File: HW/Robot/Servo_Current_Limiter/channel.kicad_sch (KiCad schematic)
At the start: 7 parts, among them J12 1x1 2.54mm male, J13 1x3 2.54mm male, Q7 IRF4905, Q8 BC548

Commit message: Something done.
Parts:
- added JP3: 1x2 2.54mm male, Connector_PinHeader_2.54mm:PinHeader_1x02_P2.54mm_Vertical, symbol Jumper:Jumper_2_Open
- added R25: 100k, For_Rasterboard:R_Axial_DIN0207_L6.3mm_D2.5mm_P7.62mm_Horizontal, symbol Device:R
- R19: value 220 -> 1k
- RV4: value 250 -> 1k
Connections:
- net +5V: now also JP3.1 (A), R25.1
- net DISABLE: now also R25.2
- net P: now also JP3.2 (B)
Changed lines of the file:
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@@
   (junction (at 206.375 82.55) (diameter 0) (color 0 0 0 0)
   )
+  (junction (at 170.18 35.56) (diameter 0) (color 0 0 0 0)
+  )
   (junction (at 177.8 43.18) (diameter 0) (color 0 0 0 0)
   )
   (junction (at 152.4 77.47) (diameter 0) (color 0 0 0 0)
   )
+  (junction (at 164.465 35.56) (diameter 0) (color 0 0 0 0)
+  )
+  (junction (at 184.785 35.56) (diameter 0) (color 0 0 0 0)
+  )
+  (junction (at 164.465 43.18) (diameter 0) (color 0 0 0 0)
+  )
   (wire (pts (xy 255.905 78.74) (xy 249.555 78.74))
     (stroke (width 0) (type default) (color 0 0 0 0))
   )
-  (wire (pts (xy 182.88 35.56) (xy 187.96 35.56))
+  (wire (pts (xy 182.88 35.56) (xy 184.785 35.56))
+    (stroke (width 0) (type default) (color 0 0 0 0))
+  )
+  (wire (pts (xy 164.465 35.56) (xy 170.18 35.56))
+    (stroke (width 0) (type default) (color 0 0 0 0))
+  )
+  (wire (pts (xy 182.245 22.225) (xy 184.785 22.225))
     (stroke (width 0) (type default) (color 0 0 0 0))
   )
@@
     (stroke (width 0) (type default) (color 0 0 0 0))
   )
+  (wire (pts (xy 184.785 22.225) (xy 184.785 35.56))
+    (stroke (width 0) (type default) (color 0 0 0 0))
+  )
   (wire (pts (xy 206.375 82.55) (xy 233.045 82.55))
     (stroke (width 0) (type default) (color 0 0 0 0))
@@
     (stroke (width 0) (type default) (color 0 0 0 0))
   )
+  (wire (pts (xy 170.18 35.56) (xy 172.72 35.56))
+    (stroke (width 0) (type default) (color 0 0 0 0))
+  )
   (wire (pts (xy 133.35 81.28) (xy 133.35 85.09))
     (stroke (width 0) (type default) (color 0 0 0 0))
@@
     (stroke (width 0) (type default) (color 0 0 0 0))
   )
+  (wire (pts (xy 164.465 43.18) (xy 177.8 43.18))
+    (stroke (width 0) (type default) (color 0 0 0 0))
+  )
   (wire (pts (xy 195.58 35.56) (xy 200.66 35.56))
     (stroke (width 0) (type default) (color 0 0 0 0))
   )
-  (wire (pts (xy 168.91 35.56) (xy 172.72 35.56))
+  (wire (pts (xy 172.085 22.225) (xy 170.18 22.225))
+    (stroke (width 0) (type default) (color 0 0 0 0))
+  )
+  (wire (pts (xy 158.115 35.56) (xy 164.465 35.56))
     (stroke (width 0) (type default) (color 0 0 0 0))
   )
@@
     (stroke (width 0) (type default) (color 0 0 0 0))
   )
+  (wire (pts (xy 170.18 22.225) (xy 170.18 35.56))
+    (stroke (width 0) (type default) (color 0 0 0 0))
+  )
   (wire (pts (xy 133.35 71.12) (xy 133.35 73.66))
     (stroke (width 0) (type default) (color 0 0 0 0))
@@
     (stroke (width 0) (type default) (color 0 0 0 0))
   )
-  (wire (pts (xy 121.92 43.18) (xy 177.8 43.18))
+  (wire (pts (xy 121.92 43.18) (xy 164.465 43.18))
+    (stroke (width 0) (type default) (color 0 0 0 0))
+  )
+  (wire (pts (xy 184.785 35.56) (xy 187.96 35.56))
     (stroke (width 0) (type default) (color 0 0 0 0))
   )
@@
     (effects (font (size 1.27 1.27)) (justify right))
   )
+  (symbol (lib_id "Device:R") (at 164.465 39.37 0) (unit 1)
+    (in_bom yes) (on_board yes)
+    (property "Reference" "R25" (id 0) (at 159.2072 39.37 90))
+    (property "Value" "100k" (id 1) (at 161.5186 39.37 90))
+    (property "Footprint" "For_Rasterboard:R_Axial_DIN0207_L6.3mm_D2.5mm_P7.62mm_Horizontal" (id 2) (at 162.687 39.37 90)
+      (effects (font (size 1.27 1.27)) hide)
+    )
+    (property "Datasheet" "~" (id 3) (at 164.465 39.37 0)
+      (effects (font (size 1.27 1.27)) hide)
+    )
+    (pin "1")
+    (pin "2")
+  )
+  (symbol (lib_id "Jumper:Jumper_2_Open") (at 177.165 22.225 0) (unit 1)
+    (in_bom yes) (on_board yes) (fields_autoplaced)
+    (property "Reference" "JP3" (id 0) (at 177.165 15.24 0))
+    (property "Value" "1x2 2.54mm male" (id 1) (at 177.165 17.78 0))
+    (property "Footprint" "Connector_PinHeader_2.54mm:PinHeader_1x02_P2.54mm_Vertical" (id 2) (at 177.165 22.225 0)
+      (effects (font (size 1.27 1.27)) hide)
+    )
+    (property "Datasheet" "~" (id 3) (at 177.165 22.225 0)
+      (effects (font (size 1.27 1.27)) hide)
+    )
+    (pin "1")
+    (pin "2")
+  )
   (symbol (lib_id "power:+5V") (at 133.35 60.96 0) (unit 1)
     (in_bom yes) (on_board yes) (fields_autoplaced)
@@
     (pin "1")
   )
-  (symbol (lib_id "power:+5V") (at 168.91 35.56 90) (unit 1)
-    (in_bom yes) (on_board yes)
-    (property "Reference" "#PWR028" (id 0) (at 172.72 35.56 0)
-      (effects (font (size 1.27 1.27)) hide)
-    )
-    (property "Value" "+5V" (id 1) (at 165.6588 35.179 90)
+  (symbol (lib_id "power:+5V") (at 158.115 35.56 90) (unit 1)
+    (in_bom yes) (on_board yes)
+    (property "Reference" "#PWR028" (id 0) (at 161.925 35.56 0)
+      (effects (font (size 1.27 1.27)) hide)
+    )
+    (property "Value" "+5V" (id 1) (at 154.8638 35.179 90)
       (effects (font (size 1.27 1.27)) (justify left))
     )
-    (property "Footprint" "" (id 2) (at 168.91 35.56 0)
-      (effects (font (size 1.27 1.27)) hide)
-    )
-    (property "Datasheet" "" (id 3) (at 168.91 35.56 0)
+    (property "Footprint" "" (id 2) (at 158.115 35.56 0)
+      (effects (font (size 1.27 1.27)) hide)
+    )
+    (property "Datasheet" "" (id 3) (at 158.115 35.56 0)
       (effects (font (size 1.27 1.27)) hide)
     )
@@
     (in_bom yes) (on_board yes)
     (property "Reference" "R19" (id 0) (at 128.0922 67.31 90))
-    (property "Value" "220" (id 1) (at 130.4036 67.31 90))
+    (property "Value" "1k" (id 1) (at 130.4036 67.31 90))
     (property "Footprint" "For_Rasterboard:R_Axial_DIN0207_L6.3mm_D2.5mm_Pinf_Horizontal" (id 2) (at 131.572 67.31 90)
       (effects (font (size 1.27 1.27)) hide)
@@
       (effects (font (size 1.27 1.27)) (justify right))
     )
-    (property "Value" "250" (id 1) (at 130.81 78.7399 0)
+    (property "Value" "1k" (id 1) (at 130.81 78.7399 0)
       (effects (font (size 1.27 1.27)) (justify right))
     )

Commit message: Working.
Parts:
- removed Q8: BC548, For_Rasterboard:TO-92_Inline_inf, symbol Servo_Current_Limiter-cache:BC548
- added R7: 1k, For_Rasterboard:R_Axial_DIN0207_L6.3mm_D2.5mm_Pinf_Horizontal, symbol Device:R
- added U1: LM324, Package_DIP:DIP-14_W7.62mm, symbol Amplifier_Operational:LM324
- renumbered JP3 to JP5, R25 to R43
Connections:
- net DISABLE: now also J12.1, RV4.2, U1.6 (-); no longer Q7.1 (G), R43.2
- net GND: now also R7.2
- net OUT: now also U1.5 (+)
- new net CTRL: Q7.1 (G), R43.2, R7.1, U1.7
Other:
- moved on the sheet: J12, R19, RV4

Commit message: Corrections.
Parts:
- R1: renamed from R19; footprint For_Rasterboard:R_Axial_DIN0207_L6.3mm_D2.5mm_Pinf_Horizontal -> For_Rasterboard:R_Axial_DIN0207_L6.3mm_D2.5mm_P5.08mm_Vertical
- renumbered J12 to J3, J13 to J4, JP5 to JP2, Q7 to Q1, R20 to R2, R43 to R25, RV4 to RV1
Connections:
- net DISABLE renamed N_DISABLE
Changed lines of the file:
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@@
     (effects (font (size 1.27 1.27)) (justify left bottom))
   )
-  (label "DISABLE" (at 117.475 111.125 180)
+  (label "N_DISABLE" (at 117.475 111.125 180)
     (effects (font (size 1.27 1.27)) (justify right bottom))
   )
@@
     (effects (font (size 1.27 1.27)) (justify left bottom))
   )
-  (hierarchical_label "DISABLE" (shape input) (at 102.87 111.125 180)
+  (hierarchical_label "N_DISABLE" (shape input) (at 102.87 111.125 180)
     (effects (font (size 1.27 1.27)) (justify right))
   )
@@
   (symbol (lib_id "Device:R") (at 164.465 39.37 0) (unit 1)
     (in_bom yes) (on_board yes)
-    (property "Reference" "R43" (id 0) (at 159.2072 39.37 90))
+    (property "Reference" "R25" (id 0) (at 159.2072 39.37 90))
     (property "Value" "100k" (id 1) (at 161.5186 39.37 90))
     (property "Footprint" "For_Rasterboard:R_Axial_DIN0207_L6.3mm_D2.5mm_P7.62mm_Horizontal" (id 2) (at 162.687 39.37 90)
@@
   (symbol (lib_id "Jumper:Jumper_2_Open") (at 177.165 22.225 0) (unit 1)
     (in_bom yes) (on_board yes) (fields_autoplaced)
-    (property "Reference" "JP5" (id 0) (at 177.165 15.24 0))
+    (property "Reference" "JP2" (id 0) (at 177.165 15.24 0))
     (property "Value" "1x2 2.54mm male" (id 1) (at 177.165 17.78 0))
     (property "Footprint" "Connector_PinHeader_2.54mm:PinHeader_1x02_P2.54mm_Vertical" (id 2) (at 177.165 22.225 0)
@@
   (symbol (lib_id "power:+5V") (at 107.95 68.58 0) (unit 1)
     (in_bom yes) (on_board yes) (fields_autoplaced)
-    (property "Reference" "#PWR026" (id 0) (at 107.95 72.39 0)
+    (property "Reference" "#PWR011" (id 0) (at 107.95 72.39 0)
       (effects (font (size 1.27 1.27)) hide)
     )
@@
   (symbol (lib_id "power:+5V") (at 158.115 35.56 90) (unit 1)
     (in_bom yes) (on_board yes)
-    (property "Reference" "#PWR028" (id 0) (at 161.925 35.56 0)
+    (property "Reference" "#PWR013" (id 0) (at 161.925 35.56 0)
       (effects (font (size 1.27 1.27)) hide)
     )
@@
   (symbol (lib_id "Connector:TestPoint") (at 127 82.55 0) (unit 1)
     (in_bom yes) (on_board yes)
-    (property "Reference" "J12" (id 0) (at 127 73.66 0))
+    (property "Reference" "J3" (id 0) (at 127 73.66 0))
     (property "Value" "1x1 2.54mm male" (id 1) (at 127 76.2 0))
     (property "Footprint" "Connector_PinHeader_2.54mm:PinHeader_1x01_P2.54mm_Vertical" (id 2) (at 127 82.55 0)
@@
   (symbol (lib_id "Device:R") (at 107.95 74.93 0) (unit 1)
     (in_bom yes) (on_board yes)
-    (property "Reference" "R19" (id 0) (at 102.6922 74.93 90))
+    (property "Reference" "R1" (id 0) (at 102.6922 74.93 90))
     (property "Value" "1k" (id 1) (at 105.0036 74.93 90))
-    (property "Footprint" "For_Rasterboard:R_Axial_DIN0207_L6.3mm_D2.5mm_Pinf_Horizontal" (id 2) (at 106.172 74.93 90)
+    (property "Footprint" "For_Rasterboard:R_Axial_DIN0207_L6.3mm_D2.5mm_P5.08mm_Vertical" (id 2) (at 106.172 74.93 90)
       (effects (font (size 1.27 1.27)) hide)
     )
@@
   (symbol (lib_id "Device:Q_PMOS_GDS") (at 177.8 38.1 270) (mirror x) (unit 1)
     (in_bom yes) (on_board yes)
-    (property "Reference" "Q7" (id 0) (at 177.8 29.4132 90))
+    (property "Reference" "Q1" (id 0) (at 177.8 29.4132 90))
     (property "Value" "IRF4905" (id 1) (at 177.8 31.7246 90))
     (property "Footprint" "Package_TO_SOT_THT:TO-220-3_Vertical" (id 2) (at 180.34 33.02 0)
@@
   (symbol (lib_id "power:GND") (at 107.95 92.71 0) (mirror y) (unit 1)
     (in_bom yes) (on_board yes)
-    (property "Reference" "#PWR027" (id 0) (at 107.95 99.06 0)
+    (property "Reference" "#PWR012" (id 0) (at 107.95 99.06 0)
       (effects (font (size 1.27 1.27)) hide)
     )
@@
   (symbol (lib_id "Device:R_Potentiometer") (at 107.95 85.09 0) (unit 1)
     (in_bom yes) (on_board yes) (fields_autoplaced)
-    (property "Reference" "RV4" (id 0) (at 105.41 83.8199 0)
+    (property "Reference" "RV1" (id 0) (at 105.41 83.8199 0)
       (effects (font (size 1.27 1.27)) (justify right))
     )
@@
   (symbol (lib_id "Device:R") (at 191.77 35.56 270) (unit 1)
     (in_bom yes) (on_board yes)
-    (property "Reference" "R20" (id 0) (at 191.77 30.3022 90))
+    (property "Reference" "R2" (id 0) (at 191.77 30.3022 90))
     (property "Value" "0.1" (id 1) (at 191.77 32.6136 90))
     (property "Footprint" "For_Rasterboard:R_Axial_DIN0207_L6.3mm_D2.5mm_P7.62mm_Horizontal" (id 2) (at 191.77 33.782 90)
@@
   (symbol (lib_id "power:GND") (at 174.625 143.51 270) (unit 1)
     (in_bom yes) (on_board yes) (fields_autoplaced)
-    (property "Reference" "#PWR029" (id 0) (at 168.275 143.51 0)
+    (property "Reference" "#PWR014" (id 0) (at 168.275 143.51 0)
       (effects (font (size 1.27 1.27)) hide)
     )
@@
   (symbol (lib_id "Connector_Generic:Conn_01x03") (at 181.61 140.97 0) (mirror x) (unit 1)
     (in_bom yes) (on_board yes)
-    (property "Reference" "J13" (id 0) (at 184.785 142.2401 0)
-      (effects (font (size 1.27 1.27)) (justify left))
-    )
+    (property "Reference" "J4" (id 0) (at 184.785 142.2401 0)
+      (effects (font (size 1.27 1.27)) (justify left))
+    )

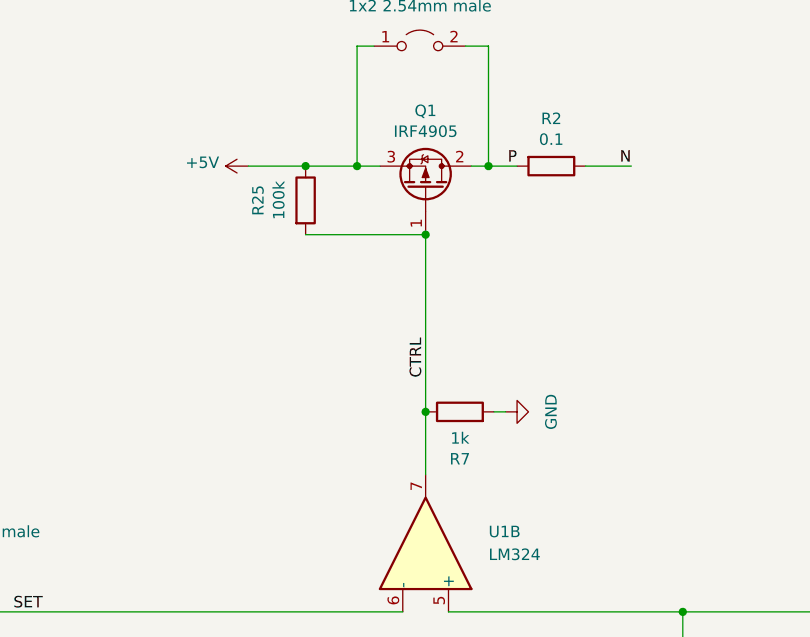
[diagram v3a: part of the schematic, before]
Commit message: Solution for offset. Now it works.
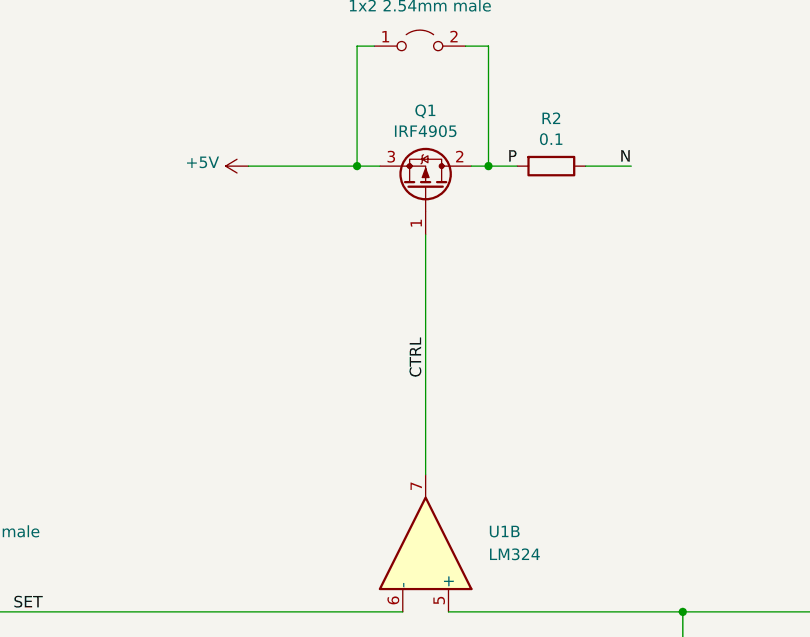
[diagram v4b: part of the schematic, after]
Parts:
- removed R25: 100k, For_Rasterboard:R_Axial_DIN0207_L6.3mm_D2.5mm_P7.62mm_Horizontal, symbol Device:R
- removed R7: 1k, For_Rasterboard:R_Axial_DIN0207_L6.3mm_D2.5mm_Pinf_Horizontal, symbol Device:R
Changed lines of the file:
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@@
   (junction (at 170.18 35.56) (diameter 0) (color 0 0 0 0)
   )
-  (junction (at 177.8 43.18) (diameter 0) (color 0 0 0 0)
-  )
   (junction (at 127 85.09) (diameter 0) (color 0 0 0 0)
   )
-  (junction (at 164.465 35.56) (diameter 0) (color 0 0 0 0)
-  )
   (junction (at 184.785 35.56) (diameter 0) (color 0 0 0 0)
   )
-  (junction (at 177.8 62.865) (diameter 0) (color 0 0 0 0)
-  )
   (wire (pts (xy 255.905 81.28) (xy 249.555 81.28))
     (stroke (width 0) (type default) (color 0 0 0 0))
@@
     (stroke (width 0) (type default) (color 0 0 0 0))
   )
-  (wire (pts (xy 164.465 35.56) (xy 170.18 35.56))
+  (wire (pts (xy 158.115 35.56) (xy 170.18 35.56))
     (stroke (width 0) (type default) (color 0 0 0 0))
   )
@@
     (stroke (width 0) (type default) (color 0 0 0 0))
   )
-  (wire (pts (xy 185.42 62.865) (xy 186.69 62.865))
-    (stroke (width 0) (type default) (color 0 0 0 0))
-  )
-  (wire (pts (xy 164.465 43.18) (xy 177.8 43.18))
-    (stroke (width 0) (type default) (color 0 0 0 0))
-  )
   (wire (pts (xy 195.58 35.56) (xy 200.66 35.56))
     (stroke (width 0) (type default) (color 0 0 0 0))
@@
     (stroke (width 0) (type default) (color 0 0 0 0))
   )
-  (wire (pts (xy 158.115 35.56) (xy 164.465 35.56))
-    (stroke (width 0) (type default) (color 0 0 0 0))
-  )
   (wire (pts (xy 174.625 143.51) (xy 176.53 143.51))
     (stroke (width 0) (type default) (color 0 0 0 0))
@@
     (stroke (width 0) (type default) (color 0 0 0 0))
   )
-  (wire (pts (xy 177.8 62.865) (xy 177.8 69.85))
+  (wire (pts (xy 177.8 43.18) (xy 177.8 69.85))
     (stroke (width 0) (type default) (color 0 0 0 0))
   )
@@
   )
   (wire (pts (xy 184.785 35.56) (xy 187.96 35.56))
-    (stroke (width 0) (type default) (color 0 0 0 0))
-  )
-  (wire (pts (xy 177.8 43.18) (xy 177.8 62.865))
     (stroke (width 0) (type default) (color 0 0 0 0))
   )
@@
   (hierarchical_label "OUT" (shape output) (at 179.705 107.95 180)
     (effects (font (size 1.27 1.27)) (justify right))
-  )
-  (symbol (lib_id "Device:R") (at 164.465 39.37 0) (unit 1)
-    (in_bom yes) (on_board yes)
-    (property "Reference" "R25" (id 0) (at 159.2072 39.37 90))
-    (property "Value" "100k" (id 1) (at 161.5186 39.37 90))
-    (property "Footprint" "For_Rasterboard:R_Axial_DIN0207_L6.3mm_D2.5mm_P7.62mm_Horizontal" (id 2) (at 162.687 39.37 90)
-      (effects (font (size 1.27 1.27)) hide)
-    )
-    (property "Datasheet" "~" (id 3) (at 164.465 39.37 0)
-      (effects (font (size 1.27 1.27)) hide)
-    )
-    (pin "1")
-    (pin "2")
   )
   (symbol (lib_id "Jumper:Jumper_2_Open") (at 177.165 22.225 0) (unit 1)
@@
     )
     (property "Datasheet" "~" (id 3) (at 177.165 22.225 0)
-      (effects (font (size 1.27 1.27)) hide)
-    )
-    (pin "1")
-    (pin "2")
-  )
-  (symbol (lib_id "Device:R") (at 181.61 62.865 90) (unit 1)
-    (in_bom yes) (on_board yes)
-    (property "Reference" "R7" (id 0) (at 181.61 68.1228 90))
-    (property "Value" "1k" (id 1) (at 181.61 65.8114 90))
-    (property "Footprint" "For_Rasterboard:R_Axial_DIN0207_L6.3mm_D2.5mm_Pinf_Horizontal" (id 2) (at 181.61 64.643 90)
-      (effects (font (size 1.27 1.27)) hide)
-    )
-    (property "Datasheet" "~" (id 3) (at 181.61 62.865 0)
       (effects (font (size 1.27 1.27)) hide)
     )
@@
       (effects (font (size 1.27 1.27)) hide)
     )
-    (pin "1")
-  )
-  (symbol (lib_id "power:GND") (at 186.69 62.865 90) (unit 1)
-    (in_bom yes) (on_board yes) (fields_autoplaced)
-    (property "Reference" "#PWR016" (id 0) (at 193.04 62.865 0)
-      (effects (font (size 1.27 1.27)) hide)
-    )
-    (property "Value" "GND" (id 1) (at 191.77 62.865 0))
-    (property "Footprint" "" (id 2) (at 186.69 62.865 0)
-      (effects (font (size 1.27 1.27)) hide)
-    )
-    (property "Datasheet" "" (id 3) (at 186.69 62.865 0)
-      (effects (font (size 1.27 1.27)) hide)
-    )
